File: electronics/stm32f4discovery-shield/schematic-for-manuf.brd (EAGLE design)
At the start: 101.6 x 105.4 mm, 44 parts, among them IC1 MAX3468CPA, IC3 LM340H-12, IC4 LM340H-12, J1 POWER_JACKSLT, Q1 BC548

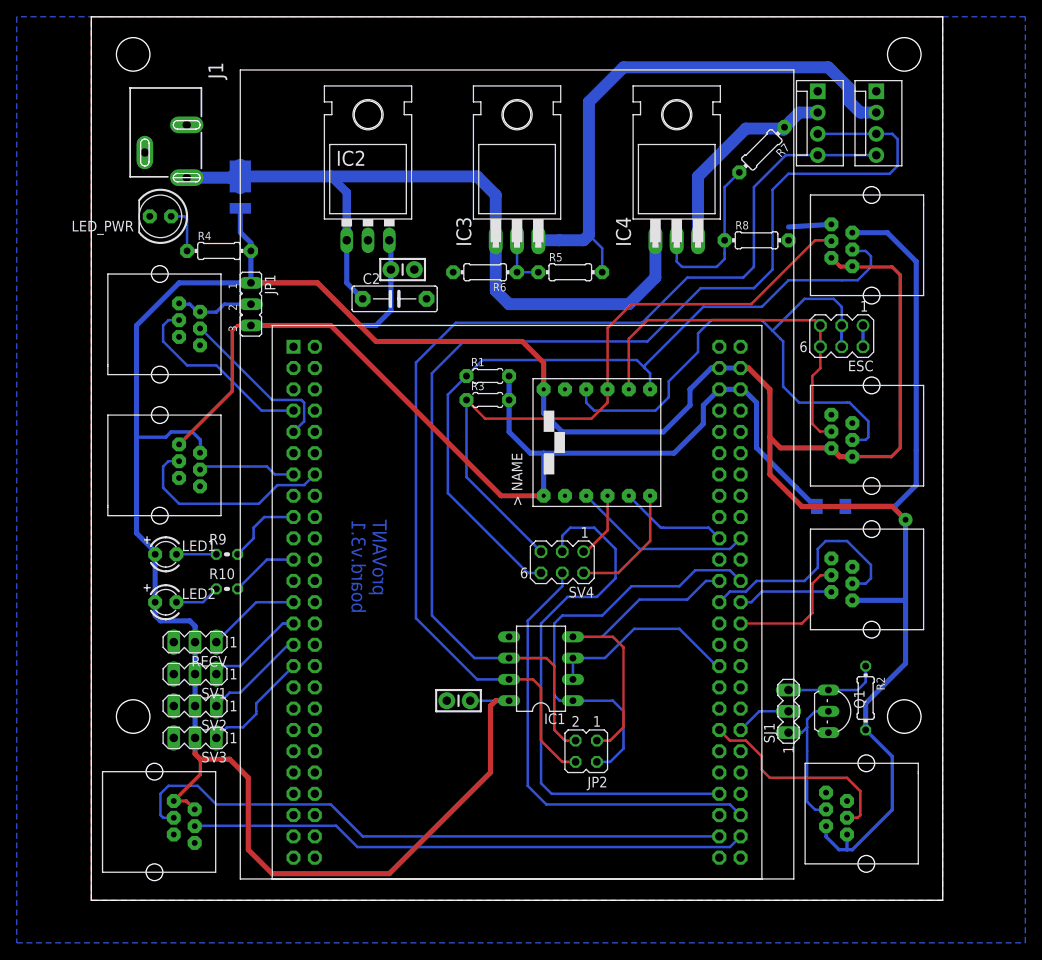
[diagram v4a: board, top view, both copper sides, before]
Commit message: Adicionados gerbers de fabricacao.
- Adicionados configuracao de CAM para o Eagle
- Adicionado tutorial de geracao de Gerbers
- Imagens renderizadas da placa (a partir dos gerbers)
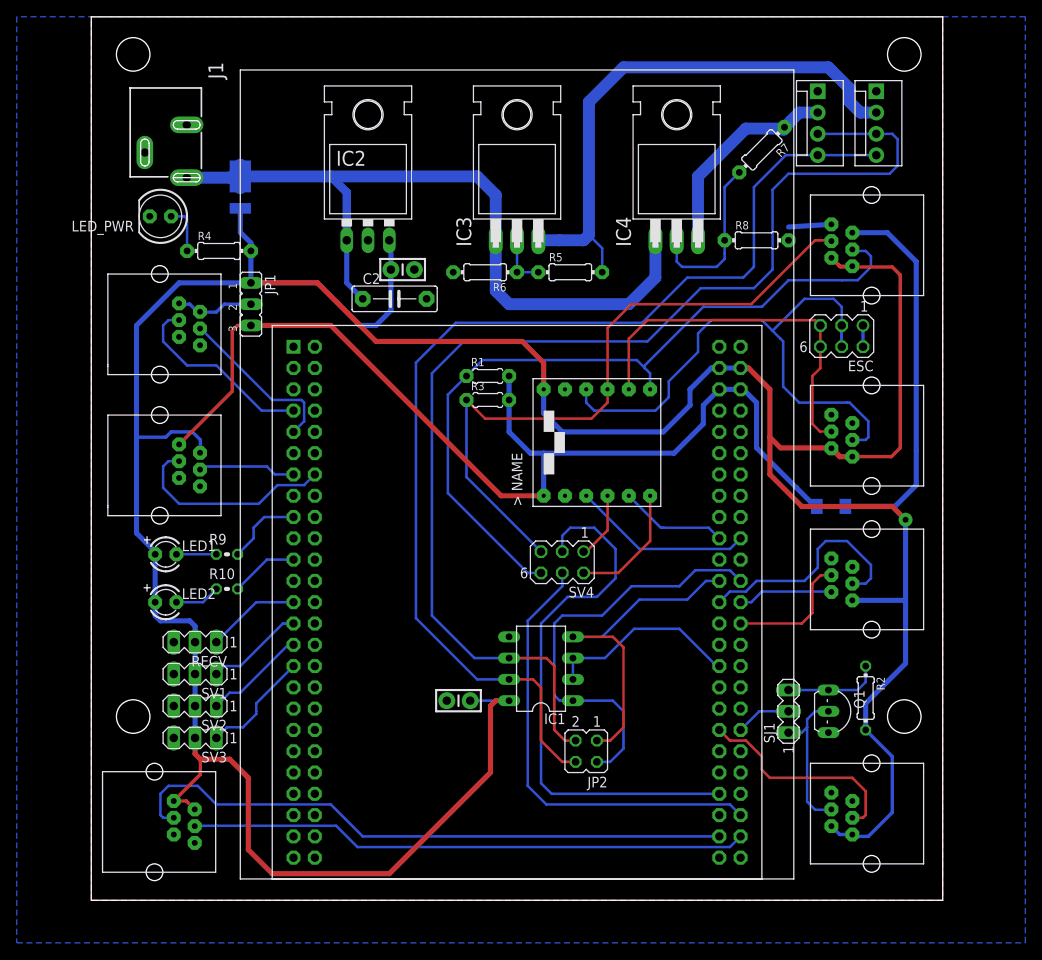
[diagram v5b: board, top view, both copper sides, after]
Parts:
- moved US3_SONAR 0.64 mm to (90.8, 14.9)
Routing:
- net 5V: track 410.9 -> 406.6 mm
- net PC10/USART3_TX: track 25.4 -> 26.0 mm
- net SONAR_RX: track 17.9 -> 18.6 mm
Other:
- board text added: "3V3 - 5V"
- board text added: "AN1"
- board text added: "ESC"
- board text added: "I2C1"
- board text added: "I2C3"
- board text added: "JP1"
- board text added: "JP2"
- board text added: "JP3"
- board text added: "PWR"
- board text added: "RECV"
- board text added: "SERVO"
- board text added: "SPI1"
- board text added: "US2"
- board text added: "US5"
- board text added: "US6"
- board text added: "proVANT board V3.2"
- board text removed: "proVANT board.v3.1"
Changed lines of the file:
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@@
 <layer number="111" name="LPC17xx" color="7" fill="1" visible="no" active="yes"/>
 <layer number="112" name="tSilk" color="7" fill="1" visible="no" active="yes"/>
+<layer number="113" name="manual_silk_top" color="11" fill="1" visible="yes" active="yes"/>
+<layer number="114" name="manual_silk_bottom" color="3" fill="1" visible="yes" active="yes"/>
 <layer number="116" name="Patch_BOT" color="9" fill="4" visible="no" active="yes"/>
 <layer number="121" name="_tsilk" color="7" fill="1" visible="no" active="yes"/>
@@
 <wire x1="80.01" y1="105.41" x2="80.01" y2="7.62" width="0.4064" layer="48"/>
 <wire x1="80.01" y1="7.62" x2="21.59" y2="7.62" width="0.4064" layer="48"/>
-<text x="35.2425" y="50.4825" size="1.6764" layer="16" rot="MR270">proVANT
-board.v3.1</text>
 <dimension x1="-8.89" y1="110.49" x2="111.76" y2="110.49" x3="51.435" y3="110.49" textsize="1.778" layer="48"/>
 <hole x="5" y="106" drill="3.999990625"/>
@@
 <hole x="97" y="106" drill="3.999990625"/>
 <hole x="97" y="27" drill="3.999990625"/>
+<text x="1.5875" y="21.2725" size="1.524" layer="113">US6</text>
+<text x="1.905" y="63.8175" size="1.524" layer="113">US2</text>
+<text x="1.905" y="80.645" size="1.524" layer="113">AN1</text>
+<text x="4.1275" y="84.1375" size="1.524" layer="113" rot="R90">PWR</text>
+<text x="62.865" y="55.88" size="1.27" layer="113" rot="R90">3V3 - 5V</text>
+<text x="95.5675" y="70.1675" size="1.524" layer="113" rot="R90">ESC</text>
+<text x="95.25" y="90.17" size="1.524" layer="113">I2C3</text>
+<text x="95.5675" y="67.6275" size="1.524" layer="113">I2C1</text>
+<text x="95.25" y="34.925" size="1.524" layer="113">SPI1</text>
+<text x="95.25" y="7.3025" size="1.524" layer="113">US5</text>
+<text x="20.955" y="80.645" size="1.524" layer="113">JP1</text>
+<text x="62.23" y="20.6375" size="1.524" layer="113">JP2</text>
+<text x="81.5975" y="32.0675" size="1.524" layer="113">JP3</text>
+<text x="34.925" y="50.165" size="1.524" layer="114" rot="MR270">proVANT
+board V3.2</text>
+<text x="99.06" y="93.98" size="1.524" layer="113" rot="R90">SERVO</text>
+<text x="1.905" y="35.2425" size="1.524" layer="113">RECV</text>
 </plain>
 <attributes>
@@
 <element name="SRVO2" library="SparkFun-Connectors" package="MOLEX-1X4" value="" x="93.6625" y="101.6" rot="R270"/>
 <element name="SPI1" library="con-tycoelectronics" package="RJ12-PROVANT" value="RJ11" x="90.805" y="42.8625" rot="R90"/>
-<element name="US3_SONAR" library="con-tycoelectronics" package="RJ12-PROVANT" value="RJ11" x="90.17" y="14.9225" rot="R90"/>
+<element name="US3_SONAR" library="con-tycoelectronics" package="RJ12-PROVANT" value="RJ11" x="90.805" y="14.9225" rot="R90"/>
 <element name="Q1" library="transistor-npn" package="TO92-EBC" value="BC548" x="89.2175" y="27.6225" rot="R270"/>
 <element name="R2" library="rcl" package="0204/7" value="" x="92.3925" y="29.21" rot="R270"/>
@@
 <contactref element="US3_SONAR" pad="P1"/>
 <contactref element="US6" pad="P1"/>
-<wire x1="80.9625" y1="65.7225" x2="80.9625" y2="60.325" width="0.6096" layer="1"/>
+<wire x1="80.9625" y1="66.04" x2="80.9625" y2="60.325" width="0.6096" layer="1"/>
 <wire x1="80.9625" y1="60.325" x2="80.9625" y2="55.88" width="0.6096" layer="1"/>
 <wire x1="80.9625" y1="55.88" x2="84.7725" y2="52.07" width="0.6096" layer="1"/>
@@
 <wire x1="92.3925" y1="28.575" x2="92.3925" y2="25.4" width="0.6096" layer="16"/>
 <wire x1="92.3925" y1="25.4" x2="92.3925" y2="25.0825" width="0.6096" layer="16"/>
-<wire x1="87.67" y1="13.9225" x2="87.67" y2="12.66" width="0.4064" layer="16"/>
-<wire x1="87.67" y1="12.66" x2="89.2175" y2="11.1125" width="0.4064" layer="16"/>
-<wire x1="89.2175" y1="11.1125" x2="90.17" y2="11.1125" width="0.4064" layer="16"/>
-<wire x1="90.17" y1="11.1125" x2="90.805" y2="11.1125" width="0.4064" layer="16"/>
-<wire x1="90.805" y1="11.1125" x2="95.5675" y2="15.875" width="0.4064" layer="16"/>
-<wire x1="95.5675" y1="15.875" x2="95.5675" y2="22.225" width="0.4064" layer="16"/>
+<wire x1="95.5675" y1="15.5575" x2="95.5675" y2="22.225" width="0.4064" layer="16"/>
 <wire x1="95.5675" y1="22.225" x2="92.3925" y2="25.4" width="0.4064" layer="16"/>
-<wire x1="80.9625" y1="65.7225" x2="80.9625" y2="66.04" width="0.6096" layer="1"/>
 <wire x1="80.9625" y1="66.04" x2="78.4225" y2="68.58" width="0.6096" layer="1"/>
 <wire x1="78.4225" y1="68.58" x2="77.47" y2="68.58" width="0.6096" layer="1"/>
@@
 <wire x1="89.305" y1="80.725" x2="90.805" y2="80.725" width="0.4064" layer="1"/>
 <wire x1="88.305" y1="81.725" x2="89.385" y2="80.645" width="0.4064" layer="1"/>
-<wire x1="89.385" y1="80.645" x2="90.805" y2="80.645" width="0.4064" layer="1"/>
-<wire x1="90.805" y1="80.645" x2="95.5675" y2="80.645" width="0.4064" layer="1"/>
+<wire x1="89.385" y1="80.645" x2="95.5675" y2="80.645" width="0.4064" layer="1"/>
 <wire x1="95.5675" y1="80.645" x2="96.52" y2="79.6925" width="0.4064" layer="1"/>
-<wire x1="96.52" y1="79.6925" x2="96.52" y2="61.9125" width="0.4064" layer="1"/>
-<wire x1="96.52" y1="61.9125" x2="96.52" y2="59.055" width="0.4064" layer="1"/>
+<wire x1="96.52" y1="79.6925" x2="96.52" y2="59.055" width="0.4064" layer="1"/>
 <wire x1="96.52" y1="59.055" x2="95.4725" y2="58.0075" width="0.4064" layer="1"/>
 <wire x1="95.4725" y1="58.0075" x2="90.805" y2="58.0075" width="0.4064" layer="1"/>
-<wire x1="90.17" y1="12.9225" x2="90.17" y2="11.1125" width="0.4064" layer="16"/>
+<wire x1="95.5675" y1="15.5575" x2="92.71" y2="12.7" width="0.4064" layer="16"/>
+<wire x1="92.71" y1="12.7" x2="91.0275" y2="12.7" width="0.4064" layer="16"/>
+<wire x1="91.0275" y1="12.7" x2="90.805" y2="12.9225" width="0.4064" layer="16"/>
+<wire x1="90.805" y1="12.9225" x2="89.305" y2="12.9225" width="0.4064" layer="16"/>
+<wire x1="89.305" y1="12.9225" x2="88.305" y2="13.9225" width="0.4064" layer="16"/>
 </signal>
 <signal name="3.3V">
@@
 <wire x1="80.01" y1="22.225" x2="80.01" y2="20.6375" width="0.3048" layer="1"/>
 <wire x1="80.01" y1="20.6375" x2="80.9625" y2="19.685" width="0.3048" layer="1"/>
-<wire x1="80.9625" y1="19.685" x2="90.17" y2="19.685" width="0.3048" layer="1"/>
-<wire x1="90.17" y1="19.685" x2="91.7575" y2="18.0975" width="0.3048" layer="1"/>
-<wire x1="91.7575" y1="18.0975" x2="91.7575" y2="15.24" width="0.3048" layer="1"/>
-<wire x1="91.7575" y1="15.24" x2="91.44" y2="14.9225" width="0.3048" layer="1"/>
-<wire x1="91.44" y1="14.9225" x2="90.17" y2="14.9225" width="0.3048" layer="1"/>
+<wire x1="80.9625" y1="19.685" x2="90.805" y2="19.685" width="0.3048" layer="1"/>
+<wire x1="90.805" y1="19.685" x2="92.3925" y2="18.0975" width="0.3048" layer="1"/>
+<wire x1="92.3925" y1="18.0975" x2="92.3925" y2="15.24" width="0.3048" layer="1"/>
+<wire x1="92.3925" y1="15.24" x2="92.075" y2="14.9225" width="0.3048" layer="1"/>
+<wire x1="92.075" y1="14.9225" x2="90.805" y2="14.9225" width="0.3048" layer="1"/>
 </signal>
 <signal name="SONAR_RX">
@@
 <wire x1="85.4075" y1="25.7175" x2="84.7725" y2="25.0825" width="0.3048" layer="16"/>
 <wire x1="84.7725" y1="25.0825" x2="83.185" y2="25.0825" width="0.3048" layer="16"/>
-<wire x1="85.4075" y1="22.86" x2="85.4075" y2="25.7175" width="0.3048" layer="16"/>
-<wire x1="85.4075" y1="22.86" x2="85.4075" y2="16.8275" width="0.3048" layer="16"/>
+<wire x1="85.4075" y1="25.7175" x2="85.4075" y2="16.8275" width="0.3048" layer="16"/>
 <wire x1="85.4075" y1="16.8275" x2="86.36" y2="15.875" width="0.3048" layer="16"/>
-<wire x1="86.36" y1="15.875" x2="87.6225" y2="15.875" width="0.3048" layer="16"/>
-<wire x1="87.6225" y1="15.875" x2="87.67" y2="15.9225" width="0.3048" layer="16"/>
+<wire x1="86.36" y1="15.875" x2="88.2575" y2="15.875" width="0.3048" layer="16"/>
+<wire x1="88.2575" y1="15.875" x2="88.305" y2="15.9225" width="0.3048" layer="16"/>
 </signal>
 <signal name="N$3">
